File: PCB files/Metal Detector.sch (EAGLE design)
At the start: 105 parts, among them IC1 NE5534AD, IC2 BQ24133RGYR, IC4 ESP32-WROOM-32UE-N4, IC6 TLV62130ARGTR, IC7 TLV1117-33IDCYR, J1 DG128-7.5, J2 DG128-7.5, Q1 IRF740, Q11 MMBT3904, Q2 IRF740, Q3 IRF9630, Q4 IRF740, Q9 MMBT3904, X2 DC21MMX

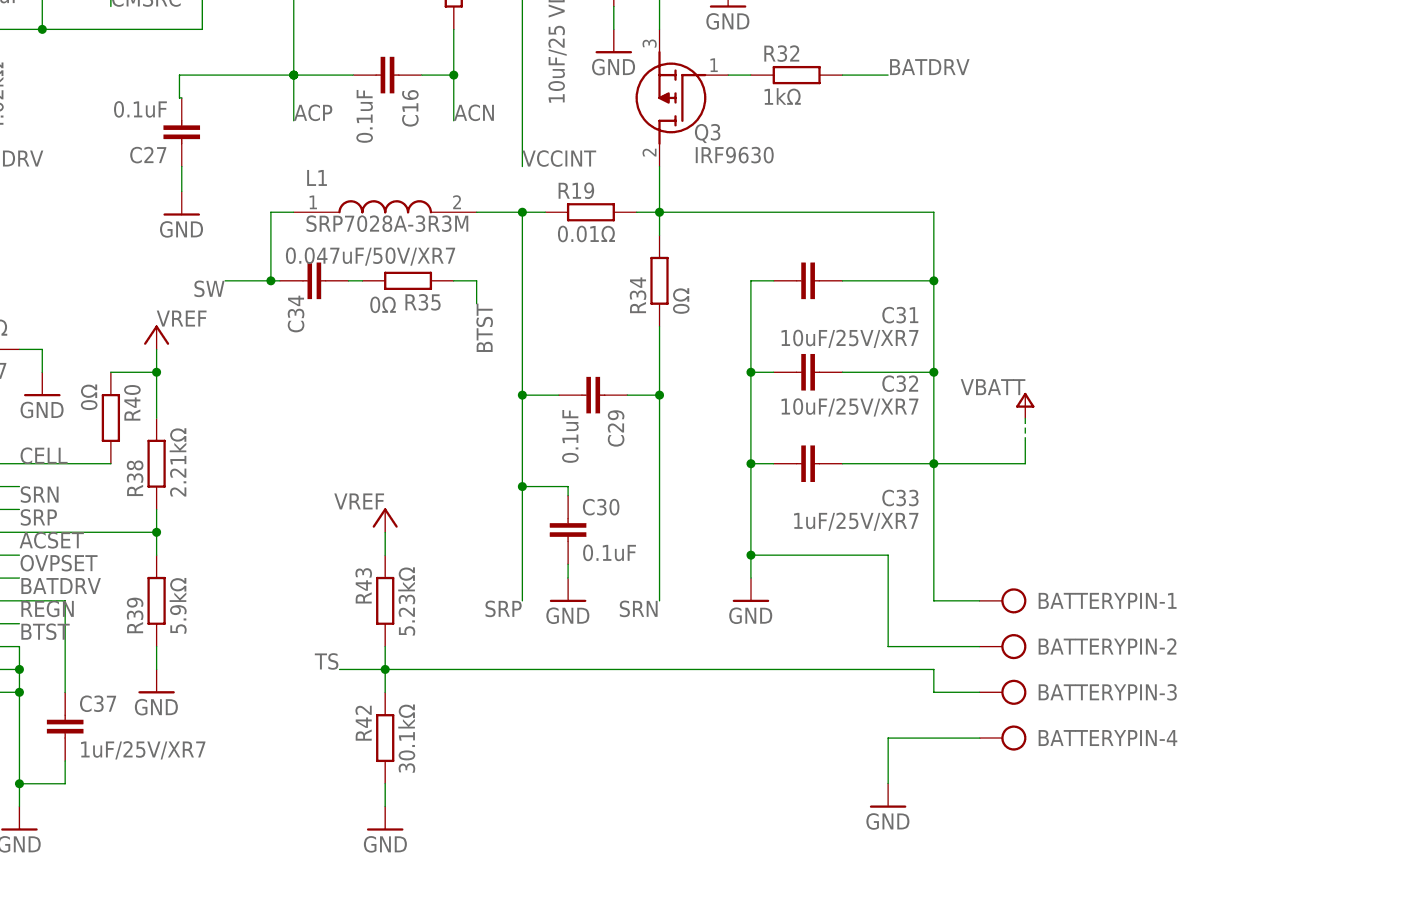
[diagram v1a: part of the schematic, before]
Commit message: Add files via upload
Battery charge circuit on design progress
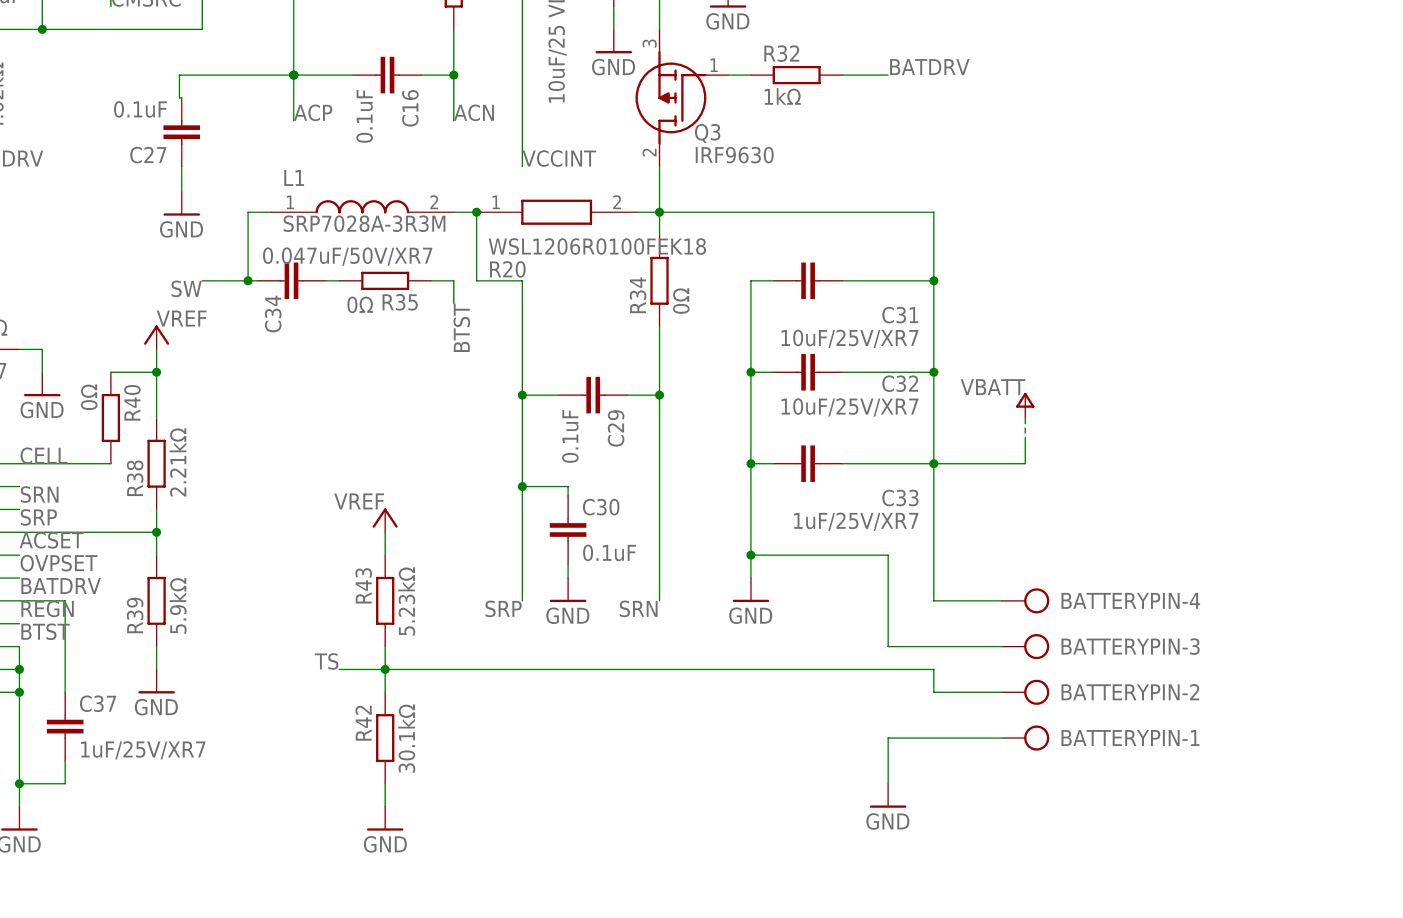
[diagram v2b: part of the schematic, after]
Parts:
- removed R19: 0.01Ω, rcl:R-EU_R2010
- added R20: WSL1206R0100FEK18, WSL1206R0100FEK18:WSL1206R0100FEK18
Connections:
- net GND: now also BATTERYPIN-1.KL, BATTERYPIN-3.KL; no longer BATTERYPIN-2.KL, BATTERYPIN-4.KL
- net SRP: now also R20.1; no longer R19.1
- net TS: now also BATTERYPIN-2.KL; no longer BATTERYPIN-3.KL
- net VBATT: now also BATTERYPIN-4.KL, R20.2; no longer BATTERYPIN-1.KL, R19.2
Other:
- moved on the sheet: BATTERYPIN-1, BATTERYPIN-2, BATTERYPIN-3, BATTERYPIN-4, C34, L1, R35
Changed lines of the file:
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@@
 <part name="R21" library="rcl" library_urn="urn:adsk.eagle:library:334" deviceset="R-EU_" device="R0603" package3d_urn="urn:adsk.eagle:package:23555/3" value="0Ω"/>
 <part name="R14" library="rcl" library_urn="urn:adsk.eagle:library:334" deviceset="R-EU_" device="R2010" package3d_urn="urn:adsk.eagle:package:23551/2" value="0.02Ω"/>
-<part name="R19" library="rcl" library_urn="urn:adsk.eagle:library:334" deviceset="R-EU_" device="R2010" package3d_urn="urn:adsk.eagle:package:23551/2" value="0.01Ω"/>
+<part name="R20" library="WSL1206R0100FEK18" deviceset="WSL1206R0100FEK18" device=""/>
 </parts>
 <sheets>
@@
 <attribute name="VALUE" x="247.396" y="446.659" size="1.778" layer="96" rot="R180"/>
 </instance>
-<instance part="L1" gate="G$1" x="177.8" y="480.06" smashed="yes">
-<attribute name="NAME" x="179.07" y="483.87" size="1.778" layer="95" align="center-left"/>
-<attribute name="VALUE" x="179.07" y="478.79" size="1.778" layer="96" align="center-left"/>
-</instance>
-<instance part="C34" gate="G$1" x="178.816" y="472.44" smashed="yes" rot="R90">
-<attribute name="NAME" x="177.165" y="470.916" size="1.778" layer="95" rot="R270"/>
-<attribute name="VALUE" x="176.784" y="474.345" size="1.778" layer="96"/>
-</instance>
-<instance part="R35" gate="G$1" x="190.5" y="472.44" smashed="yes" rot="R180">
-<attribute name="NAME" x="194.31" y="470.9414" size="1.778" layer="95" rot="R180"/>
-<attribute name="VALUE" x="189.23" y="470.662" size="1.778" layer="96" rot="R180"/>
+<instance part="L1" gate="G$1" x="175.26" y="480.06" smashed="yes">
+<attribute name="NAME" x="176.53" y="483.87" size="1.778" layer="95" align="center-left"/>
+<attribute name="VALUE" x="176.53" y="478.79" size="1.778" layer="96" align="center-left"/>
+</instance>
+<instance part="C34" gate="G$1" x="176.276" y="472.44" smashed="yes" rot="R90">
+<attribute name="NAME" x="174.625" y="470.916" size="1.778" layer="95" rot="R270"/>
+<attribute name="VALUE" x="174.244" y="474.345" size="1.778" layer="96"/>
+</instance>
+<instance part="R35" gate="G$1" x="187.96" y="472.44" smashed="yes" rot="R180">
+<attribute name="NAME" x="191.77" y="470.9414" size="1.778" layer="95" rot="R180"/>
+<attribute name="VALUE" x="186.69" y="470.662" size="1.778" layer="96" rot="R180"/>
 </instance>
 <instance part="C35" gate="G$1" x="226.06" y="510.54" smashed="yes">
@@
 <attribute name="VALUE" x="530.606" y="500.253" size="1.778" layer="96" rot="R180"/>
 </instance>
-<instance part="BATTERYPIN" gate="-1" x="259.08" y="436.88" smashed="yes" rot="MR0">
-<attribute name="NAME" x="260.35" y="437.769" size="1.778" layer="95" rot="MR180"/>
-</instance>
-<instance part="BATTERYPIN" gate="-2" x="259.08" y="431.8" smashed="yes" rot="MR0">
-<attribute name="NAME" x="260.35" y="432.689" size="1.778" layer="95" rot="MR180"/>
-</instance>
-<instance part="BATTERYPIN" gate="-3" x="259.08" y="426.72" smashed="yes" rot="MR0">
-<attribute name="NAME" x="260.35" y="427.609" size="1.778" layer="95" rot="MR180"/>
-</instance>
-<instance part="BATTERYPIN" gate="-4" x="259.08" y="421.64" smashed="yes" rot="MR0">
-<attribute name="NAME" x="260.35" y="422.529" size="1.778" layer="95" rot="MR180"/>
-<attribute name="VALUE" x="262.89" y="417.957" size="1.778" layer="96" rot="MR0"/>
+<instance part="BATTERYPIN" gate="-1" x="261.62" y="421.64" smashed="yes" rot="R180">
+<attribute name="NAME" x="262.89" y="420.751" size="1.778" layer="95"/>
+</instance>
+<instance part="BATTERYPIN" gate="-2" x="261.62" y="426.72" smashed="yes" rot="R180">
+<attribute name="NAME" x="262.89" y="425.831" size="1.778" layer="95"/>
+</instance>
+<instance part="BATTERYPIN" gate="-3" x="261.62" y="431.8" smashed="yes" rot="R180">
+<attribute name="NAME" x="262.89" y="430.911" size="1.778" layer="95"/>
+</instance>
+<instance part="BATTERYPIN" gate="-4" x="261.62" y="436.88" smashed="yes" rot="R180">
+<attribute name="NAME" x="262.89" y="435.991" size="1.778" layer="95"/>
+<attribute name="VALUE" x="265.43" y="440.563" size="1.778" layer="96" rot="R180"/>
 </instance>
 <instance part="GND12" gate="1" x="243.84" y="414.02" smashed="yes">
@@
 <attribute name="VALUE" x="184.15" y="514.858" size="1.778" layer="96"/>
 </instance>
-<instance part="R19" gate="G$1" x="210.82" y="480.06" smashed="yes">
-<attribute name="NAME" x="207.01" y="481.5586" size="1.778" layer="95"/>
-<attribute name="VALUE" x="207.01" y="476.758" size="1.778" layer="96"/>
+<instance part="R20" gate="G$1" x="198.12" y="480.06" smashed="yes">
+<attribute name="NAME" x="199.39" y="473.71" size="1.778" layer="95" align="center-left"/>
+<attribute name="VALUE" x="199.39" y="476.25" size="1.778" layer="96" align="center-left"/>
 </instance>
 </instances>
@@
 <wire x1="243.84" y1="441.96" x2="228.6" y2="441.96" width="0.1524" layer="91"/>
 <junction x="228.6" y="441.96"/>
-<pinref part="BATTERYPIN" gate="-2" pin="KL"/>
-<wire x1="243.84" y1="431.8" x2="254" y2="431.8" width="0.1524" layer="91"/>
+<pinref part="BATTERYPIN" gate="-3" pin="KL"/>
+<wire x1="256.54" y1="431.8" x2="243.84" y2="431.8" width="0.1524" layer="91"/>
 </segment>
 <segment>
@@
 <wire x1="243.84" y1="421.64" x2="243.84" y2="416.56" width="0.1524" layer="91"/>
 <pinref part="GND12" gate="1" pin="GND"/>
-<pinref part="BATTERYPIN" gate="-4" pin="KL"/>
-<wire x1="243.84" y1="421.64" x2="254" y2="421.64" width="0.1524" layer="91"/>
+<pinref part="BATTERYPIN" gate="-1" pin="KL"/>
+<wire x1="256.54" y1="421.64" x2="243.84" y2="421.64" width="0.1524" layer="91"/>
 </segment>
 </net>
@@
 <wire x1="248.92" y1="429.26" x2="187.96" y2="429.26" width="0.1524" layer="91"/>
 <wire x1="248.92" y1="426.72" x2="248.92" y2="429.26" width="0.1524" layer="91"/>
-<pinref part="BATTERYPIN" gate="-3" pin="KL"/>
-<wire x1="248.92" y1="426.72" x2="254" y2="426.72" width="0.1524" layer="91"/>
+<pinref part="BATTERYPIN" gate="-2" pin="KL"/>
+<wire x1="256.54" y1="426.72" x2="248.92" y2="426.72" width="0.1524" layer="91"/>
 </segment>
 </net>
@@
 <wire x1="208.28" y1="448.564" x2="208.28" y2="449.58" width="0.1524" layer="91"/>
 <label x="203.2" y="436.88" size="1.778" layer="95" rot="R180"/>
+<wire x1="203.2" y1="459.74" x2="203.2" y2="472.44" width="0.1524" layer="91"/>
+<junction x="203.2" y="459.74"/>
+<wire x1="203.2" y1="472.44" x2="198.12" y2="472.44" width="0.1524" layer="91"/>
 <pinref part="L1" gate="G$1" pin="2"/>
-<wire x1="205.74" y1="480.06" x2="203.2" y2="480.06" width="0.1524" layer="91"/>
-<wire x1="203.2" y1="480.06" x2="198.12" y2="480.06" width="0.1524" layer="91"/>
-<wire x1="203.2" y1="459.74" x2="203.2" y2="480.06" width="0.1524" layer="91"/>
-<junction x="203.2" y="459.74"/>
-<junction x="203.2" y="480.06"/>
-<pinref part="R19" gate="G$1" pin="1"/>
+<pinref part="R20" gate="G$1" pin="1"/>
+<wire x1="195.58" y1="480.06" x2="198.12" y2="480.06" width="0.1524" layer="91"/>
+<wire x1="198.12" y1="472.44" x2="198.12" y2="480.06" width="0.1524" layer="91"/>
+<junction x="198.12" y="480.06"/>
 </segment>
 </net>
@@
 <segment>
 <pinref part="R35" gate="G$1" pin="1"/>
-<wire x1="195.58" y1="472.44" x2="198.12" y2="472.44" width="0.1524" layer="91"/>
-<wire x1="198.12" y1="472.44" x2="198.12" y2="469.9" width="0.1524" layer="91"/>
-<label x="198.12" y="469.9" size="1.778" layer="95" rot="R270"/>
+<wire x1="193.04" y1="472.44" x2="195.58" y2="472.44" width="0.1524" layer="91"/>
+<wire x1="195.58" y1="472.44" x2="195.58" y2="469.9" width="0.1524" layer="91"/>
+<label x="195.58" y="469.9" size="1.778" layer="95" rot="R270"/>
 </segment>
 </net>
@@
 <wire x1="248.92" y1="452.12" x2="259.08" y2="452.12" width="0.1524" layer="91"/>
 <wire x1="259.08" y1="452.12" x2="259.08" y2="454.66" width="0.1524" layer="91"/>
-<pinref part="BATTERYPIN" gate="-1" pin="KL"/>
-<wire x1="248.92" y1="436.88" x2="254" y2="436.88" width="0.1524" layer="91"/>
 <pinref part="Q3" gate="G$1" pin="D"/>
-<pinref part="R19" gate="G$1" pin="2"/>
+<pinref part="BATTERYPIN" gate="-4" pin="KL"/>
+<wire x1="256.54" y1="436.88" x2="248.92" y2="436.88" width="0.1524" layer="91"/>
+<pinref part="R20" gate="G$1" pin="2"/>
 </segment>
 </net>
@@
 <net name="SW" class="0">
 <segment>
-<label x="170.18" y="472.44" size="1.778" layer="95" rot="R180"/>
+<label x="167.64" y="472.44" size="1.778" layer="95" rot="R180"/>
 <pinref part="C34" gate="G$1" pin="1"/>
-<wire x1="175.26" y1="472.44" x2="170.18" y2="472.44" width="0.1524" layer="91"/>
-<wire x1="176.276" y1="472.44" x2="175.26" y2="472.44" width="0.1524" layer="91"/>
+<wire x1="172.72" y1="472.44" x2="167.64" y2="472.44" width="0.1524" layer="91"/>
+<wire x1="173.736" y1="472.44" x2="172.72" y2="472.44" width="0.1524" layer="91"/>
 <pinref part="L1" gate="G$1" pin="1"/>
-<wire x1="177.8" y1="480.06" x2="175.26" y2="480.06" width="0.1524" layer="91"/>
-<wire x1="175.26" y1="480.06" x2="175.26" y2="472.44" width="0.1524" layer="91"/>
-<junction x="175.26" y="472.44"/>
+<wire x1="175.26" y1="480.06" x2="172.72" y2="480.06" width="0.1524" layer="91"/>
+<wire x1="172.72" y1="480.06" x2="172.72" y2="472.44" width="0.1524" layer="91"/>
+<junction x="172.72" y="472.44"/>
 </segment>
 <segment>
@@
 <pinref part="C34" gate="G$1" pin="2"/>
 <pinref part="R35" gate="G$1" pin="2"/>
-<wire x1="183.896" y1="472.44" x2="185.42" y2="472.44" width="0.1524" layer="91"/>
-</segment>
-</net>
+<wire x1="181.356" y1="472.44" x2="182.88" y2="472.44" width="0.1524" layer="91"/>
+</segment>
+</net>

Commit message: Add files via upload
Removed all component ot board
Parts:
- removed R14: 0.02Ω, rcl:R-EU_R2010
- removed R3, R8: 10kΩ, rcl:R-EU_0207/10
- removed R4: 2.2kΩ, rcl:R-EU_0207/10
- added R19: 20Ω, rcl:R-EU_R1206
- added R30, R31: 10KΩ, rcl:R-EU_R1206
- added R33: 2.2kΩ, rcl:R-EU_R1206
- R1: value 20Ω -> WSL1206R0200FEK18; device rcl:R-EU_0207/10 -> WSL1206R0100FEK18:WSL1206R0100FEK18
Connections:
- net ACP: now also R1.1; no longer R14.1
- net GND: now also R30.1; no longer R3.2
- net IO27: now also R33.2; no longer R4.2
- net N$1: now also R31.2; no longer R8.1
- net N$2: now also R19.2; no longer R1.2
- net N$3: now also R19.1, R30.2; no longer R1.1, R3.1
- net N$5: now also R33.1; no longer R4.1
- net N$7: now also R31.1; no longer R8.2
- net VCCINT: now also R1.2; no longer R14.2

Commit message: Add files via upload
Optimizated PCB trace and designed 12V to 5V Buck coneventer
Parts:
- removed BATTERYPIN: (no value), con-ptr500:AK300/4
- added BATTERY: (no value), con-ptr500:AK500/4
- DISPLAY: device con-amp-mt:L09P -> con-amp-mt:S09P
- ENCODER: device con-amp-mt:L05P -> con-amp-mt:S05P
- HEADPHONE: device con-amp-mt:L04P -> con-amp-mt:S04P
- SERIAL: device con-amp-mt:L06P -> con-amp-mt:S06P
- SPEAKER: device con-amp-mt:L02P -> con-amp-mt:S02P
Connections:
- net GND: now also BATTERY-1.KL, BATTERY-3.KL; no longer BATTERYPIN-1.KL, BATTERYPIN-3.KL
- net TS: now also BATTERY-2.KL; no longer BATTERYPIN-2.KL
- net VBATT: now also BATTERY-4.KL; no longer BATTERYPIN-4.KL

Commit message: Add files via upload
Redesign 5V buck conventer circuit for implementation problem
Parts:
- removed IC6: TLV62130ARGTR, TLV62130ARGTR:TLV62130ARGTR
- removed J1: DG128-7.5, DG128-7.5-02P-14-00AH:DG128-7.5-02P-14-00AH
- removed L3: IHLP2525CZER220M11, IHLP2525CZER220M11:IHLP2525CZER220M11
- removed R25: 680kΩ, rcl:R-EU_R1206
- removed R44: 130kΩ, rcl:R-EU_R1206
- added C21: 5pF, rcl:C-EUC0603
- added C22: 3300pF, rcl:C-EUC0603
- added C25, C26: 22uF, SparkFun-Capacitors:1.0UF-1206-50V-10%
- added C8: 10uF/25V, rcl:C-EUC1210
- added IC3: TPS54228DDAR, TPS54228DDAR:TPS54228DDAR
- added L2: SRP1265A-4R7M, SRP1265A-4R7M:SRP1265A-4R7M
- added ON-OFF: (no value), con-amp-mt:S02P
- added R3: 22.1kΩ, rcl:R-EU_R0603
- added R4: 124kΩ, rcl:R-EU_R0603
- C11: value 3300pF -> 0.1uF
- C14: value 22uF/6.3V -> 15pF; device rcl:C-EUC0805 -> rcl:C-EUC0603
- R24: value 100kΩ -> 10kΩ
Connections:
- removed net N$28: IC6.PG, R24.1
- removed net N$49: IC6.SW_1, IC6.SW_2, IC6.SW_3, L3.1
- removed net VCCINT: C28.1, C35.1, IC2.PVCC_1, IC2.PVCC_2, J1.2, Q3.S, R1.2, R21.1
- new net N$17: IC3.EN, R24.1
- new net N$18: C11.1, IC3.VBST
- new net N$24: C14.1, IC3.VFB, R3.2, R4.1
- new net N$33: C22.1, IC3.SS
- new net ON-OFF: ON-OFF-1.S, R24.2
- net GND: now also C21.2, C22.2, C25.2, C26.2, C8.2, IC3.EP, IC3.GND, R3.1; no longer C11.2, C14.1, IC6.AGND, IC6.DEF, IC6.EXPOSED_THERMAL_PAD, IC6.FSW, IC6.PGND_1, IC6.PGND_2, R44.2
- net N$19: now also C11.2, IC3.SW, L2.1; no longer C11.1, IC6.SS/TR
- net N$30: now also C21.1, IC3.VREG5; no longer IC6.FB, R25.2, R44.1
- net VCC: now also C25.1, C26.1, C28.1, C35.1, C8.1, IC2.PVCC_1, IC2.PVCC_2, IC3.VIN, L2.2, ON-OFF-2.S, Q3.S, R1.2, R21.1, R4.2; no longer IC6.AVIN, IC6.EN, IC6.PVIN_1, IC6.PVIN_2, IC6.VOS, J1.1, L3.2, R24.2, R25.1
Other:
- moved on the sheet: C10, C11, C13, C14, R24
